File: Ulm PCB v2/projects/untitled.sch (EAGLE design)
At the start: 27 parts, among them U1 FT232RLSSOP, U2 MCP73831, U3 SPX3819-3.3, U4 RFM69HCW, X3 microUSB

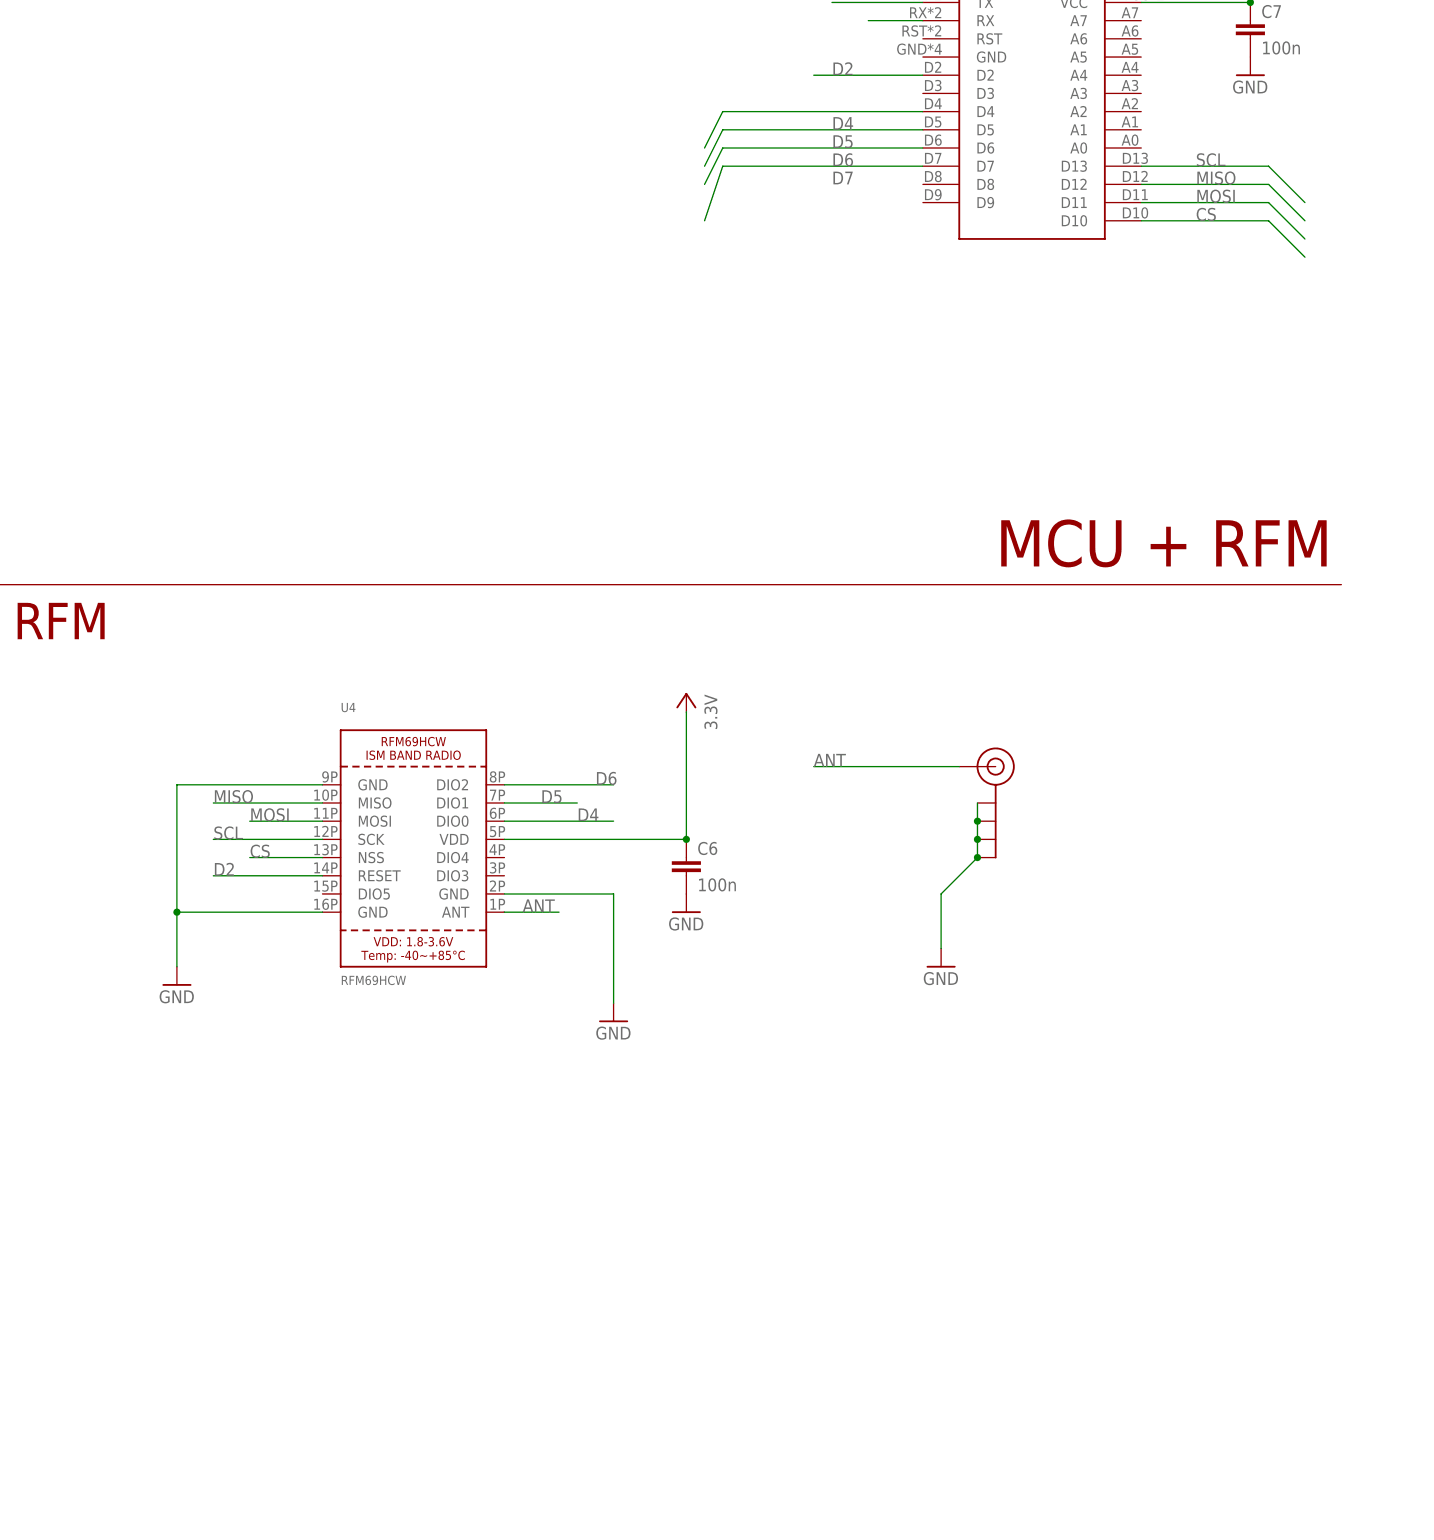
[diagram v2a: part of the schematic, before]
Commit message: added battery voltage monitoring
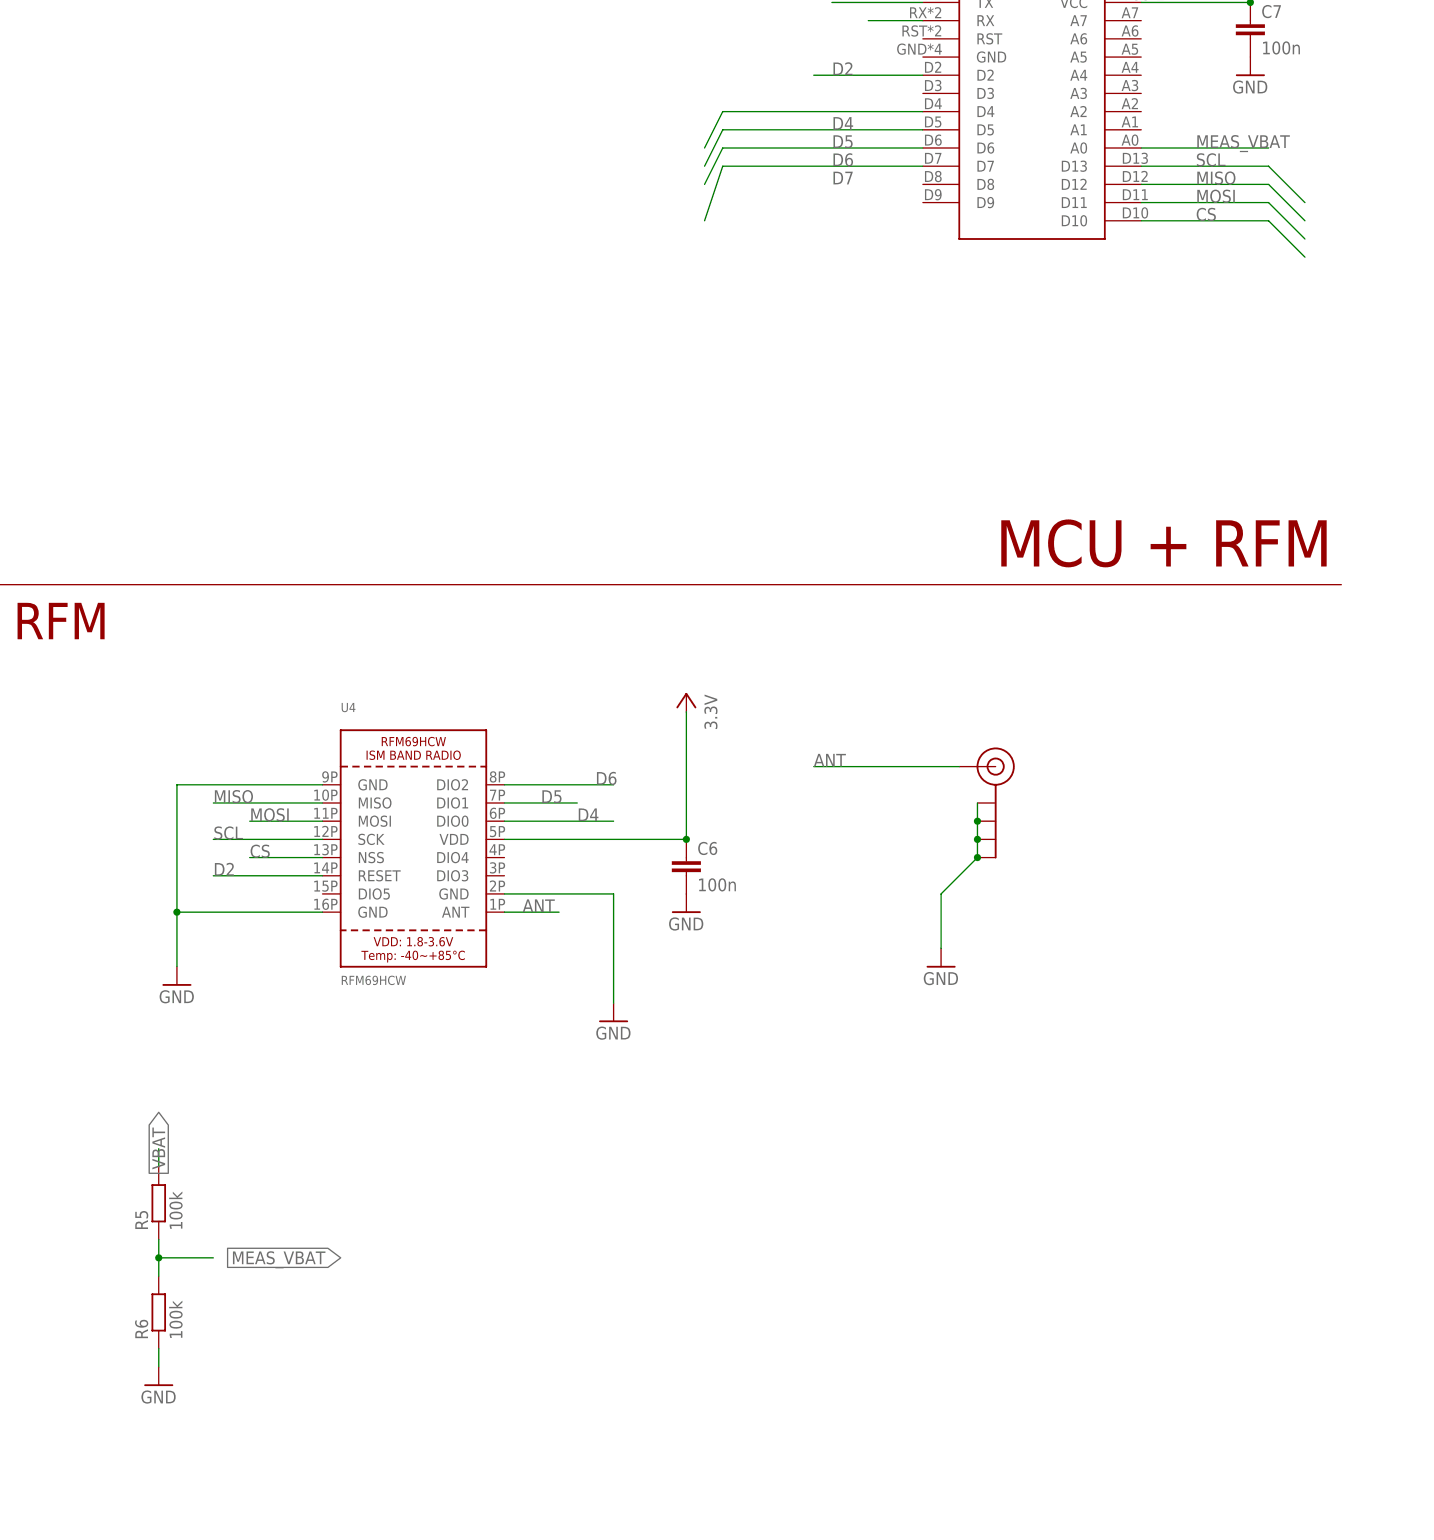
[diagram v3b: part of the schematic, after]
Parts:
- added R5, R6: 100k, rcl:R-EU_R0805
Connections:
- new net MEAS_VBAT: R5.1, R6.2, U$1.A0
- net GND: now also R6.1
- net VBAT: now also R5.2
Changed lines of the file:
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@@
 <?xml version="1.0" encoding="utf-8"?>
 <!DOCTYPE eagle SYSTEM "eagle.dtd">
-<eagle version="8.3.1">
+<eagle version="9.0.1">
 <drawing>
 <settings>
@@
 <layers>
 <layer number="1" name="Top" color="4" fill="1" visible="no" active="no"/>
+<layer number="2" name="Route2" color="1" fill="3" visible="no" active="no"/>
+<layer number="3" name="Route3" color="4" fill="3" visible="no" active="no"/>
+<layer number="4" name="Route4" color="1" fill="4" visible="no" active="no"/>
+<layer number="5" name="Route5" color="4" fill="4" visible="no" active="no"/>
+<layer number="6" name="Route6" color="1" fill="8" visible="no" active="no"/>
+<layer number="7" name="Route7" color="4" fill="8" visible="no" active="no"/>
+<layer number="8" name="Route8" color="1" fill="2" visible="no" active="no"/>
+<layer number="9" name="Route9" color="4" fill="2" visible="no" active="no"/>
+<layer number="10" name="Route10" color="1" fill="7" visible="no" active="no"/>
+<layer number="11" name="Route11" color="4" fill="7" visible="no" active="no"/>
+<layer number="12" name="Route12" color="1" fill="5" visible="no" active="no"/>
+<layer number="13" name="Route13" color="4" fill="5" visible="no" active="no"/>
+<layer number="14" name="Route14" color="1" fill="6" visible="no" active="no"/>
+<layer number="15" name="Route15" color="4" fill="6" visible="no" active="no"/>
 <layer number="16" name="Bottom" color="1" fill="1" visible="no" active="no"/>
 <layer number="17" name="Pads" color="2" fill="1" visible="no" active="no"/>
@@
 <part name="+3V2" library="supply1" deviceset="+3V3" device="" value="3.3V"/>
 <part name="X3" library="microbuilder" deviceset="USB" device="_MICRO_20329_V2" value="microUSB"/>
+<part name="R5" library="rcl" library_urn="urn:adsk.eagle:library:334" deviceset="R-EU_" device="R0805" package3d_urn="urn:adsk.eagle:package:23553/2" value="100k"/>
+<part name="R6" library="rcl" library_urn="urn:adsk.eagle:library:334" deviceset="R-EU_" device="R0805" package3d_urn="urn:adsk.eagle:package:23553/2" value="100k"/>
+<part name="GND6" library="supply1" library_urn="urn:adsk.eagle:library:371" deviceset="GND" device=""/>
 </parts>
 <sheets>
@@
 <instance part="+3V2" gate="G$1" x="121.92" y="320.04" rot="MR0"/>
 <instance part="X3" gate="G$1" x="-152.4" y="248.92"/>
+<instance part="R5" gate="G$1" x="48.26" y="248.92" rot="R90"/>
+<instance part="R6" gate="G$1" x="48.26" y="233.68" rot="R90"/>
+<instance part="GND6" gate="1" x="48.26" y="223.52"/>
 </instances>
 <busses>
@@
 <pinref part="GND10" gate="1" pin="GND"/>
 </segment>
+<segment>
+<pinref part="R6" gate="G$1" pin="1"/>
+<wire x1="48.26" y1="228.6" x2="48.26" y2="226.06" width="0.1524" layer="91"/>
+<pinref part="GND6" gate="1" pin="GND"/>
+</segment>
 </net>
 <net name="USB_D-" class="0">
@@
 <label x="0" y="309.88" size="1.778" layer="95" rot="R180" xref="yes"/>
 <pinref part="J2" gate="G$1" pin="+"/>
+</segment>
+<segment>
+<pinref part="R5" gate="G$1" pin="2"/>
+<wire x1="48.26" y1="254" x2="48.26" y2="256.54" width="0.1524" layer="91"/>
+<label x="48.26" y="261.62" size="1.778" layer="95" rot="R270" xref="yes"/>
 </segment>
 </net>
@@
 <junction x="-147.32" y="416.56"/>
 <pinref part="D3" gate="G$1" pin="C"/>
+</segment>
+</net>
+<net name="MEAS_VBAT" class="0">
+<segment>
+<pinref part="R5" gate="G$1" pin="1"/>
+<pinref part="R6" gate="G$1" pin="2"/>
+<wire x1="48.26" y1="243.84" x2="48.26" y2="241.3" width="0.1524" layer="91"/>
+<wire x1="48.26" y1="241.3" x2="48.26" y2="238.76" width="0.1524" layer="91"/>
+<wire x1="48.26" y1="241.3" x2="55.88" y2="241.3" width="0.1524" layer="91"/>
+<junction x="48.26" y="241.3"/>
+<label x="73.66" y="241.3" size="1.778" layer="95" rot="R180" xref="yes"/>
+</segment>
+<segment>
+<pinref part="U$1" gate="G$1" pin="A0"/>
+<wire x1="185.42" y1="396.24" x2="203.2" y2="396.24" width="0.1524" layer="91"/>
+<label x="193.04" y="396.24" size="1.778" layer="95"/>
 </segment>
 </net>
@@
 packages will not be understood (or retained) with this version.
 </note>
+<note version="8.4" severity="warning">
+Since Version 8.4, EAGLE supports properties for SPICE simulation.
+Probes in schematics and SPICE mapping objects found in parts and library devices
+will not be understood with this version. Update EAGLE to the latest version
+for full support of SPICE simulation.
+</note>
 </compatibility>
